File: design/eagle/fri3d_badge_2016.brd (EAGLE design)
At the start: 76.6 x 67.3 mm, 43 parts, among them Q1 MOSFET-NCHANNEL2N7002PW, U1 MCP73831

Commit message: cleaned up silk
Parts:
- moved U$7 3.81 mm to (22.0, 31.3)
- moved Q1 1.50 mm to (49.2, 50.9)
- moved C1 1.10 mm to (27.1, 41.5)
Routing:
- net GND: track 56.1 -> 53.3 mm
- net N$24: track 78.4 -> 75.8 mm
- net SCK: track 16.2 -> 14.0 mm
- net IR_TX: track 25.7 -> 24.2 mm
- net MISO: track 14.0 -> 13.1 mm
- net MOSI: track 24.4 -> 23.6 mm

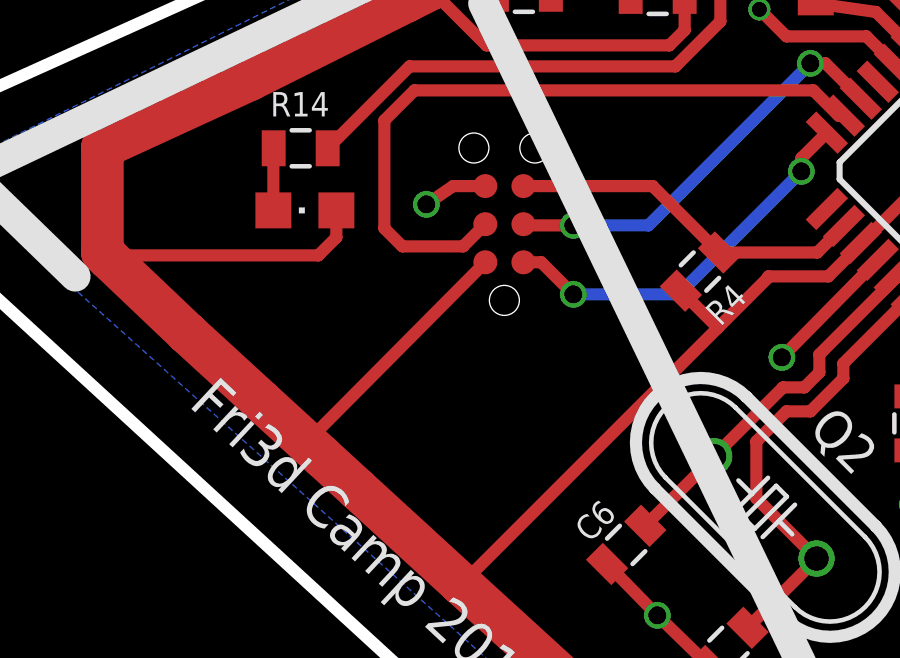
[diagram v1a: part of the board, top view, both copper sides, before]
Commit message: redid Tag Connect mapping (same layout)
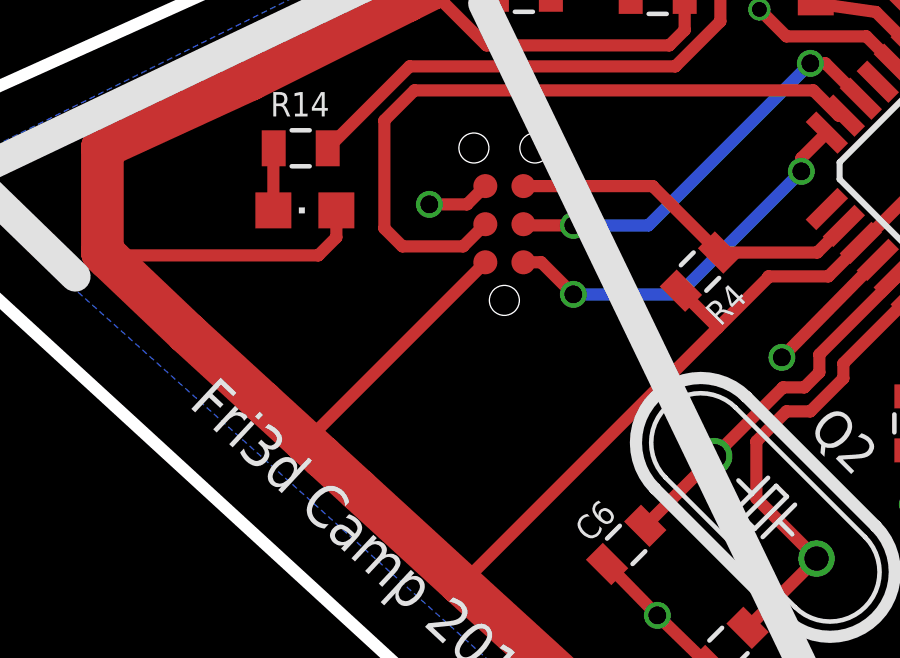
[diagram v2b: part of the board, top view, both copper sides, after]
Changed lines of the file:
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@@
 <wire x1="36.4" y1="53.3" x2="36.95" y2="53.3" width="1.016" layer="1"/>
 <wire x1="43.05" y1="53.3" x2="43.6" y2="53.3" width="1.016" layer="1"/>
-<contactref element="U$7" pad="P$4"/>
-<wire x1="21.365" y1="35.11" x2="20.29" y2="35.11" width="0.4064" layer="1"/>
-<wire x1="20.29" y1="35.11" x2="19.4" y2="34.5" width="0.4064" layer="1"/>
-<via x="19.4" y="34.5" extent="1-16" drill="0.6"/>
 <wire x1="26.2" y1="42.5" x2="26.21" y2="42.5" width="0.4064" layer="1"/>
 <wire x1="26.21" y1="42.5" x2="26.21" y2="41.45" width="0.4064" layer="1"/>
 <wire x1="49.83" y1="49.975" x2="50.425" y2="49.975" width="0.4064" layer="1"/>
 <wire x1="50.425" y1="49.975" x2="51.1" y2="49.3" width="0.4064" layer="1"/>
+<contactref element="U$7" pad="P$4"/>
+<wire x1="21.365" y1="35.11" x2="20.755" y2="34.5" width="0.4064" layer="1"/>
+<wire x1="20.755" y1="34.5" x2="19.5" y2="34.5" width="0.4064" layer="1"/>
+<via x="19.5" y="34.5" extent="1-16" drill="0.6"/>
 </signal>
 <signal name="D+">
@@
 <wire x1="20.566103125" y1="21.835621875" x2="17.124059375" y2="24.989740625" width="1.4224" layer="1"/>
 <wire x1="17.124059375" y1="24.989740625" x2="15.92386875" y2="26.089534375" width="1.4224" layer="1"/>
-<wire x1="15.92386875" y1="26.089534375" x2="13.94015625" y2="27.907309375" width="1.4224" layer="1"/>
+<wire x1="15.92386875" y1="26.089534375" x2="15.380303125" y2="26.58763125" width="1.4224" layer="1"/>
+<wire x1="15.380303125" y1="26.58763125" x2="13.94015625" y2="27.907309375" width="1.4224" layer="1"/>
 <wire x1="13.94015625" y1="27.907309375" x2="11.4356125" y2="30.202346875" width="1.4224" layer="1"/>
 <wire x1="11.4356125" y1="30.202346875" x2="8.809965625" y2="32.70025" width="1.4224" layer="1"/>
@@
 <wire x1="37.471615625" y1="8.40499375" x2="37.471615625" y2="12.528384375" width="1.016" layer="1"/>
 <wire x1="37.471615625" y1="12.528384375" x2="37.4" y2="12.6" width="1.016" layer="1"/>
-<contactref element="U$7" pad="P$6"/>
 <wire x1="15.8" y1="32.8" x2="8.909715625" y2="32.8" width="0.4064" layer="1"/>
 <wire x1="8.909715625" y1="32.8" x2="8.809965625" y2="32.70025" width="0.4064" layer="1"/>
 <wire x1="17.384740625" y1="24.989740625" x2="17.124059375" y2="24.989740625" width="0.4064" layer="1"/>
-<wire x1="21.365" y1="32.57" x2="15.604334375" y2="26.77" width="0.4064" layer="1"/>
 <wire x1="15.604334375" y1="26.77" x2="15.92386875" y2="26.089534375" width="0.4064" layer="1"/>
 <wire x1="15.8" y1="32.8" x2="16.4" y2="33.4" width="0.4064" layer="1"/>
@@
 <wire x1="27.99" y1="45.0999" x2="27.99" y2="41.47" width="0.4064" layer="1"/>
 <wire x1="27.99" y1="41.47" x2="28.01" y2="41.45" width="0.4064" layer="1"/>
+<contactref element="U$7" pad="P$6"/>
+<wire x1="21.365" y1="32.57" x2="15.38263125" y2="26.58763125" width="0.4064" layer="1"/>
+<wire x1="15.38263125" y1="26.58763125" x2="15.380303125" y2="26.58763125" width="0.4064" layer="1"/>
 </signal>
 <signal name="N$5">
@@
 <signal name="MOSI">
 <contactref element="U$1" pad="10"/>
-<contactref element="U$7" pad="P$5"/>
-<wire x1="21.365" y1="33.84" x2="20.625" y2="33.1" width="0.4064" layer="1"/>
 <wire x1="20.625" y1="33.1" x2="18.6" y2="33.1" width="0.4064" layer="1"/>
 <wire x1="18.6" y1="33.1" x2="18" y2="33.7" width="0.4064" layer="1"/>
@@
 <wire x1="32.3" y1="38.3" x2="33.141525" y2="37.458475" width="0.4064" layer="1"/>
 <wire x1="33.141525" y1="37.458475" x2="33.3160375" y2="37.458475" width="0.4064" layer="1"/>
+<contactref element="U$7" pad="P$5"/>
+<wire x1="21.365" y1="33.84" x2="20.625" y2="33.1" width="0.4064" layer="1"/>
 </signal>
 <signal name="RST">
@@
 <wire x1="29.15639375" y1="32.89639375" x2="32.430909375" y2="32.89639375" width="0.4064" layer="1"/>
 <wire x1="32.430909375" y1="32.89639375" x2="33.3160375" y2="33.781521875" width="0.4064" layer="1"/>
+<wire x1="29.15639375" y1="32.89639375" x2="26.9427875" y2="35.11" width="0.4064" layer="1"/>
 <contactref element="U$7" pad="P$3"/>
-<wire x1="29.15639375" y1="32.89639375" x2="26.9427875" y2="35.11" width="0.4064" layer="1"/>
-<wire x1="26.9427875" y1="35.11" x2="22.635" y2="35.11" width="0.4064" layer="1"/>
+<wire x1="22.635" y1="35.11" x2="26.9427875" y2="35.11" width="0.4064" layer="1"/>
 </signal>
 <signal name="SCK">
 <contactref element="U$1" pad="9"/>
-<contactref element="U$7" pad="P$2"/>
 <via x="24.3" y="33.8" extent="1-16" drill="0.6"/>
 <via x="32.2" y="39.2" extent="1-16" drill="0.6"/>
 <wire x1="32.2" y1="39.2" x2="32.705884375" y2="39.2" width="0.4064" layer="1"/>
 <wire x1="32.705884375" y1="39.2" x2="33.881721875" y2="38.0241625" width="0.4064" layer="1"/>
+<wire x1="24.3" y1="33.8" x2="26.8" y2="33.8" width="0.4064" layer="16"/>
+<wire x1="26.8" y1="33.8" x2="32.2" y2="39.2" width="0.4064" layer="16"/>
+<contactref element="U$7" pad="P$2"/>
 <wire x1="22.635" y1="33.84" x2="22.675" y2="33.8" width="0.4064" layer="1"/>
 <wire x1="22.675" y1="33.8" x2="24.3" y2="33.8" width="0.4064" layer="1"/>
-<wire x1="24.3" y1="33.8" x2="26.8" y2="33.8" width="0.4064" layer="16"/>
-<wire x1="26.8" y1="33.8" x2="32.2" y2="39.2" width="0.4064" layer="16"/>
 </signal>
 <signal name="MISO">
 <contactref element="U$1" pad="11"/>
-<contactref element="U$7" pad="P$1"/>
 <via x="24.3" y="31.5" extent="1-16" drill="0.6"/>
 <via x="31.9" y="35.6" extent="1-16" drill="0.6"/>
 <wire x1="31.9" y1="35.6" x2="31.9" y2="36.0424375" width="0.4064" layer="1"/>
 <wire x1="31.9" y1="36.0424375" x2="32.750353125" y2="36.892790625" width="0.4064" layer="1"/>
-<wire x1="22.635" y1="32.57" x2="23.23" y2="32.57" width="0.4064" layer="1"/>
 <wire x1="23.23" y1="32.57" x2="24.3" y2="31.5" width="0.4064" layer="1"/>
 <wire x1="24.3" y1="31.5" x2="27.8" y2="31.5" width="0.4064" layer="16"/>
 <wire x1="27.8" y1="31.5" x2="31.9" y2="35.6" width="0.4064" layer="16"/>
+<contactref element="U$7" pad="P$1"/>
+<wire x1="22.635" y1="32.57" x2="23.23" y2="32.57" width="0.4064" layer="1"/>
 </signal>
 <signal name="N$6">
@@
 </signal>
 </signals>
+<errors>
+</errors>
 </board>
 </drawing>
